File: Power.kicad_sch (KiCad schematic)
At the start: 1 part, among them U6 18650_DUAL_HOLDER

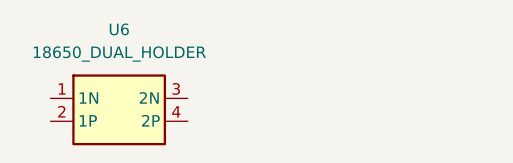
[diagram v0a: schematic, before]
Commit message: Receiver design
Updated the receiver design for the SX1280.
Added an ignore for lock files.
Minor schematic updates.
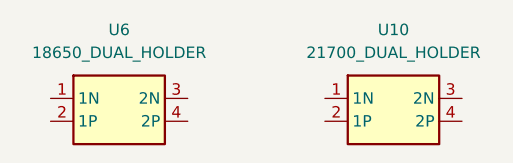
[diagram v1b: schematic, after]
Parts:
- added U10: 21700_DUAL_HOLDER, Custom_Parts:21700_DUAL_HOLDER, symbol Custom_Parts:21700_DUAL_HOLDER
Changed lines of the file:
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@@
+		)
+	)
+	(symbol
+		(lib_id "Custom_Parts:21700_DUAL_HOLDER")
+		(at 82.55 64.77 0)
+		(unit 1)
+		(exclude_from_sim no)
+		(in_bom yes)
+		(on_board yes)
+		(dnp no)
+		(fields_autoplaced yes)
+		(property "Reference" "U10"
+			(at 92.71 57.15 0)
+			(effects
+				(font
+					(size 1.27 1.27)
+				)
+			)
+		)
+		(property "Value" "21700_DUAL_HOLDER"
+			(at 92.71 59.69 0)
+			(effects
+				(font
+					(size 1.27 1.27)
+				)
+			)
+		)
+		(property "Footprint" "Custom_Parts:21700_DUAL_HOLDER"
+			(at 104.14 159.69 0)
+			(effects
+				(font
+					(size 1.27 1.27)
+				)
+				(justify left top)
+				(hide yes)
+			)
+		)
+		(property "Datasheet" "http://www.keyelco.com/product-pdf.cfm?p=920"
+			(at 104.14 259.69 0)
+			(effects
+				(font
+					(size 1.27 1.27)
+				)
+				(justify left top)
+				(hide yes)
+			)
+		)
+		(property "Description" "KEYSTONE - 1048 - BATTERY HOLDER, 18650 LI-ION, 2CELL, SMD"
+			(at 82.804 74.422 0)
+			(effects
+				(font
+					(size 1.27 1.27)
+				)
+				(hide yes)
+			)
+		)
+		(property "Height" ""
+			(at 104.14 459.69 0)
+			(effects
+				(font
+					(size 1.27 1.27)
+				)
+				(justify left top)
+				(hide yes)
+			)
+		)
+		(property "Mouser Part Number" "534-1048"
+			(at 104.14 559.69 0)
+			(effects
+				(font
+					(size 1.27 1.27)
+				)
+				(justify left top)
+				(hide yes)
+			)
+		)
+		(property "Mouser Price/Stock" "https://www.mouser.co.uk/ProductDetail/Keystone-Electronics/1048?qs=%2F7TOpeL5Mz5jXkg8vI8Dyw%3D%3D"
+			(at 104.14 659.69 0)
+			(effects
+				(font
+					(size 1.27 1.27)
+				)
+				(justify left top)
+				(hide yes)
+			)
+		)
+		(property "Manufacturer_Name" "Keystone Electronics"
+			(at 104.14 759.69 0)
+			(effects
+				(font
+					(size 1.27 1.27)
+				)
+				(justify left top)
+				(hide yes)
+			)
+		)
+		(property "Manufacturer_Part_Number" "1048"
+			(at 104.14 859.69 0)
+			(effects
+				(font
+					(size 1.27 1.27)
+				)
+				(justify left top)
+				(hide yes)
+			)
+		)
+		(pin "3"
+		)
+		(pin "2"
+		)
+		(pin "1"
+		)
+		(pin "4"
+		)
+		(instances
+			(project ""
+				(path "/ac187c6c-fa53-41cc-bce1-6f39a42a92e8/9df2a240-d97e-494f-85fd-6467f59fa68d"
+					(reference "U10")
+					(unit 1)
+				)
+			)
 		)
 	)

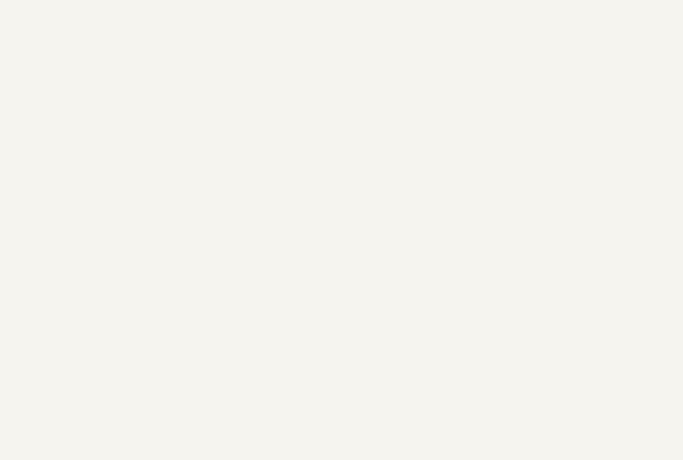
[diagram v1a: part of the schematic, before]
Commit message: Sensors design
Updated the inertial measurement unit schematic.
Updated the power monitor schematic.
Updated the barometer schematic.
Updated the receiver schematic.

TODO:
Review the sensors schematic.
Implement ESC schematic.
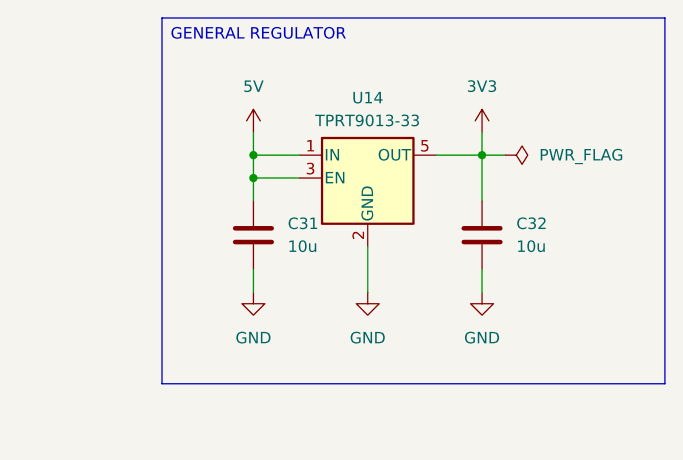
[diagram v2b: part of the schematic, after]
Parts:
- added C31, C32: 10u, symbol Device:C
- added U14: TPRT9013-33, Package_TO_SOT_SMD:SOT-23-5, symbol Regulator_Linear:TLV70233_SOT23-5
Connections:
- new net 3V3: C32.1, U14.5 (OUT)
- new net 5V: C31.1, U14.1 (IN), U14.3 (EN)
- new net GND: C31.2, C32.2, U14.2 (GND)

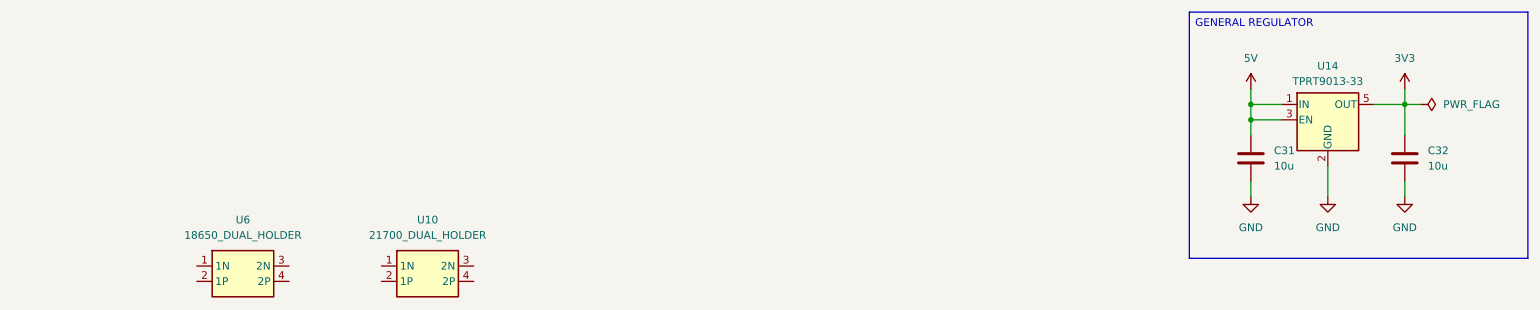
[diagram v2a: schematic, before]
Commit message: ESC design
Updated the ESC schematic.
Replaces the INA 226 with INA230.
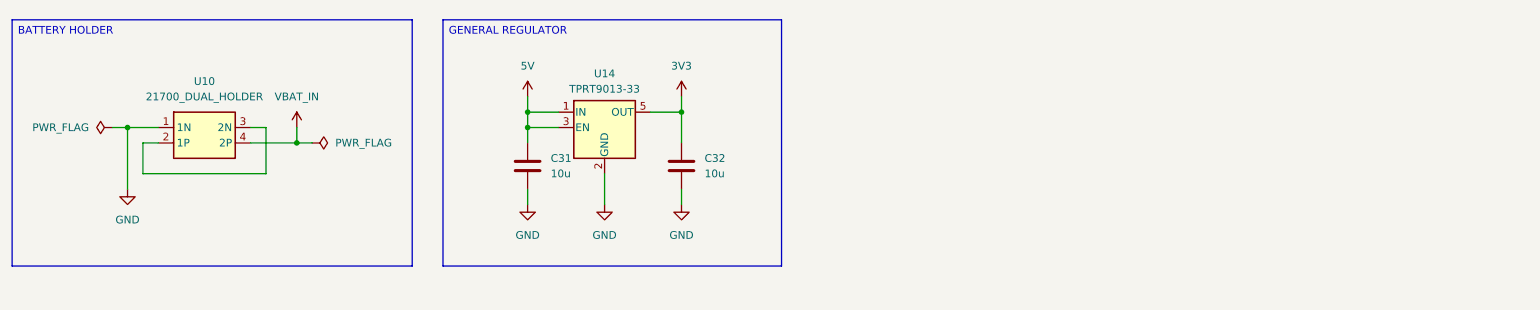
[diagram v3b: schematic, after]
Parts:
- removed U6: 18650_DUAL_HOLDER, Custom_Parts:18650_DUAL_HOLDER, symbol Custom_Parts:18650_DUAL_HOLDER
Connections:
- net GND: now also U10.1 (1N)
- net at U10.2 (1P): now also U10.3 (2N)
- net VBAT_IN: now reaches U10.4 (2P)
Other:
- moved on the sheet: C31, C32, U10, U14

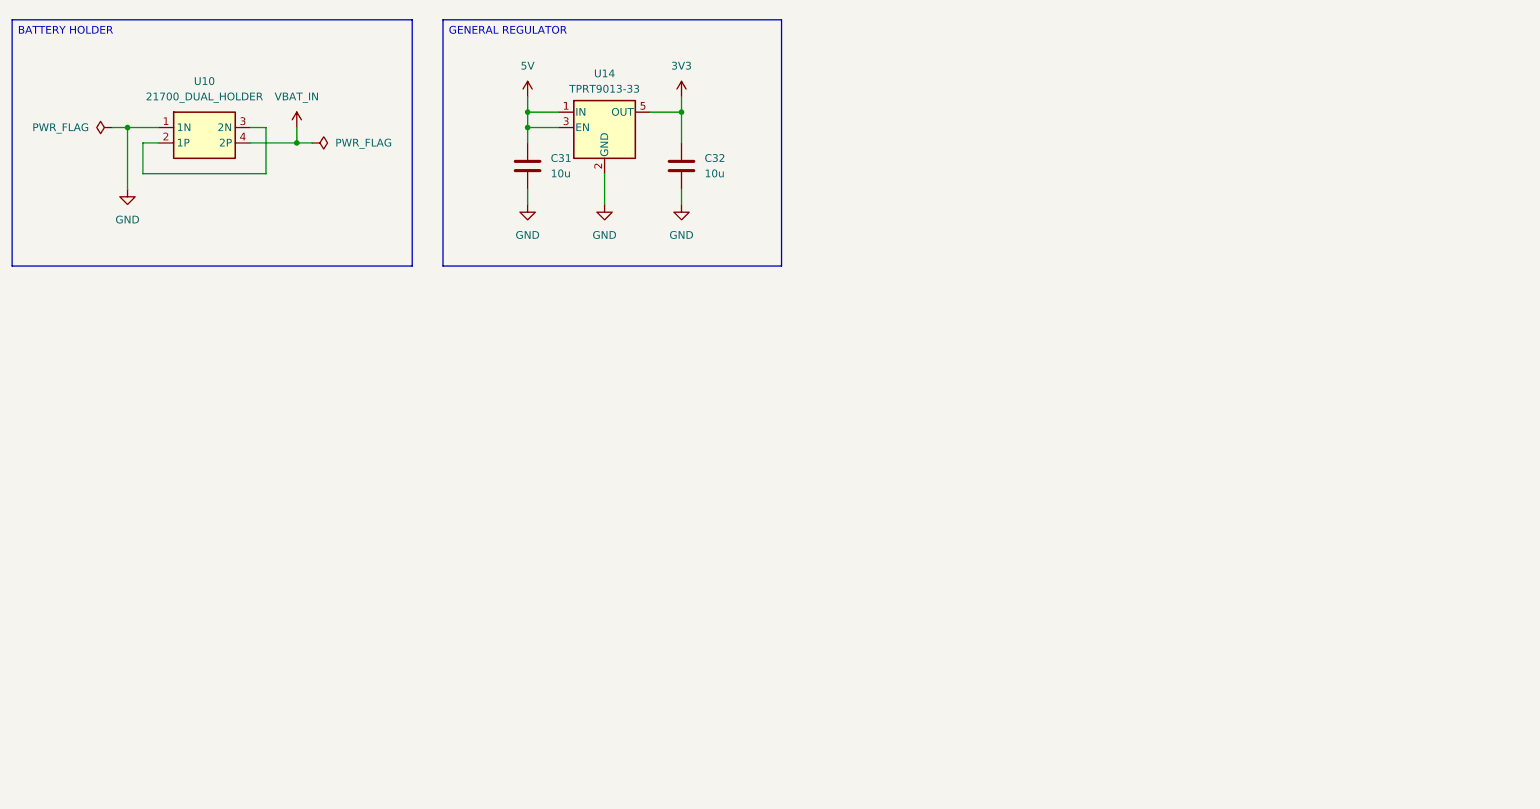
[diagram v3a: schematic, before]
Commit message: Power design
Added the 5V regulator schematic.
Updated the MCU schematic.
Updated the RX schematic.
Updated the sensors schematic.

TODO:
Calculate the voltage divider for the 5V regulator.
Review all connections and systems.
Select the footprints for the missing components.
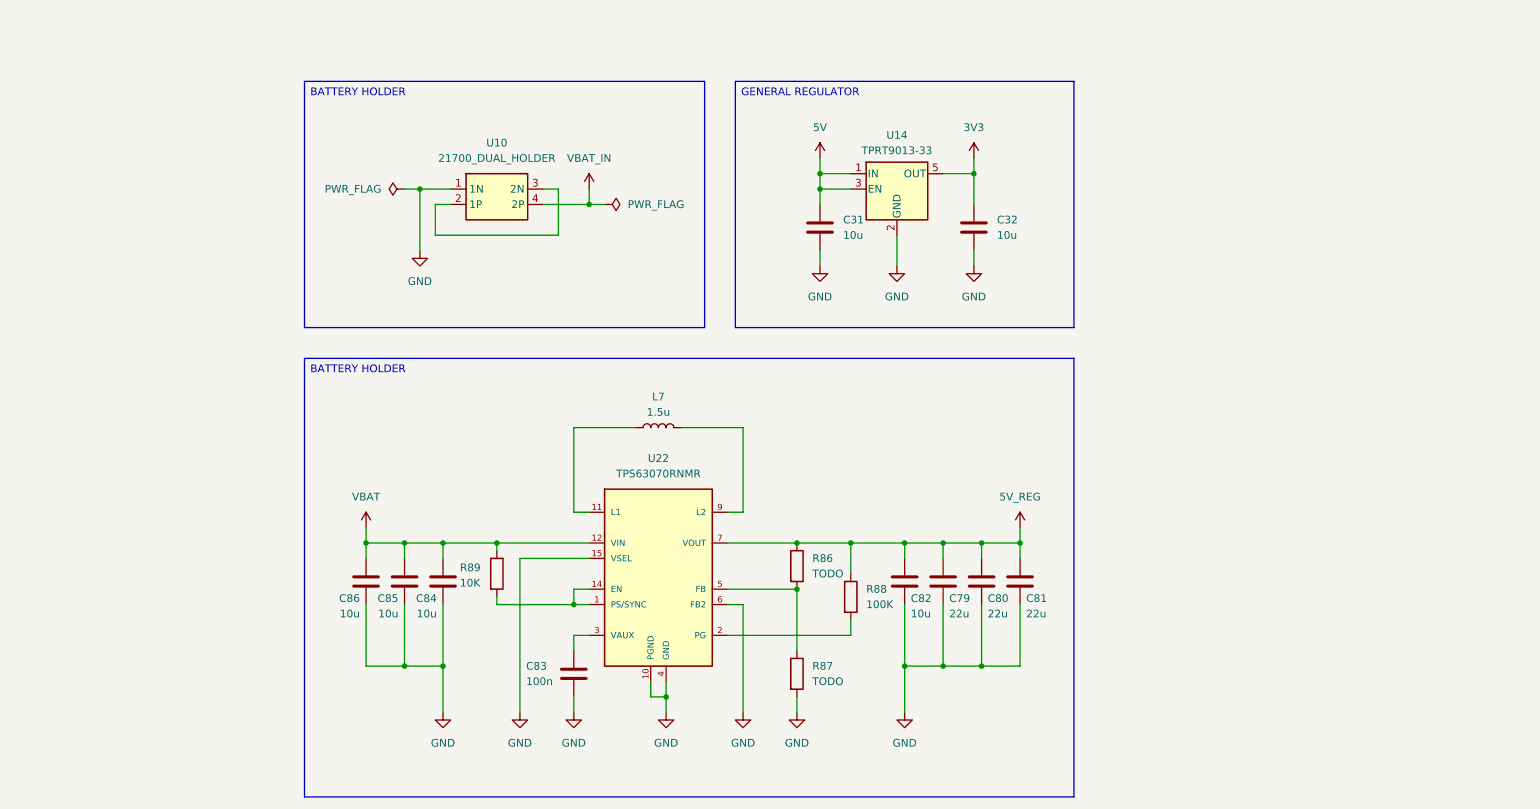
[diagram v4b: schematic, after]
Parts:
- added C79, C80, C81: 22u, symbol Device:C
- added C82, C84, C85, C86: 10u, symbol Device:C
- added C83: 100n, symbol Device:C
- added L7: 1.5u, symbol Device:L
- added R86, R87: TODO, symbol Device:R
- added R88: 100K, symbol Device:R
- added R89: 10K, symbol Device:R
- added U22: TPS63070RNMR, Custom_Parts:TPS63070RNMR, symbol Custom_Parts:TPS63070RNMR
- U10: footprint Custom_Parts:21700_DUAL_HOLDER -> Custom_Parts:21700_DUAL_HOLDER_MOUNTING
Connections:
- net GND: now also C79.2, C80.2, C81.2, C82.2, C83.2, C84.2, C85.2, C86.2, R87.2, U22.10 (PGND), U22.15 (VSEL), U22.4 (GND), U22.6 (FB2)
- new net: R89.2, U22.1 (PS/SYNC), U22.14 (EN)
- new net: L7.1, U22.11 (L1)
- new net: L7.2, U22.9 (L2)
- new net: R88.2, U22.2 (PG)
- new net: R86.2, R87.1, U22.5 (FB)
- new net: C83.1, U22.3 (VAUX)
- new net 5V_REG: C79.1, C80.1, C81.1, C82.1, R86.1, R88.1, U22.7 (VOUT)
- new net VBAT: C84.1, C85.1, C86.1, R89.1, U22.12 (VIN)
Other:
- moved on the sheet: C31, C32, U10, U14

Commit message: Footprints and revision
Added the missing footprints.
Updated a all the schematics.
Completed an initial review of the schematics.

TODO:
Perform a deep review of the schematics before committing to layout.
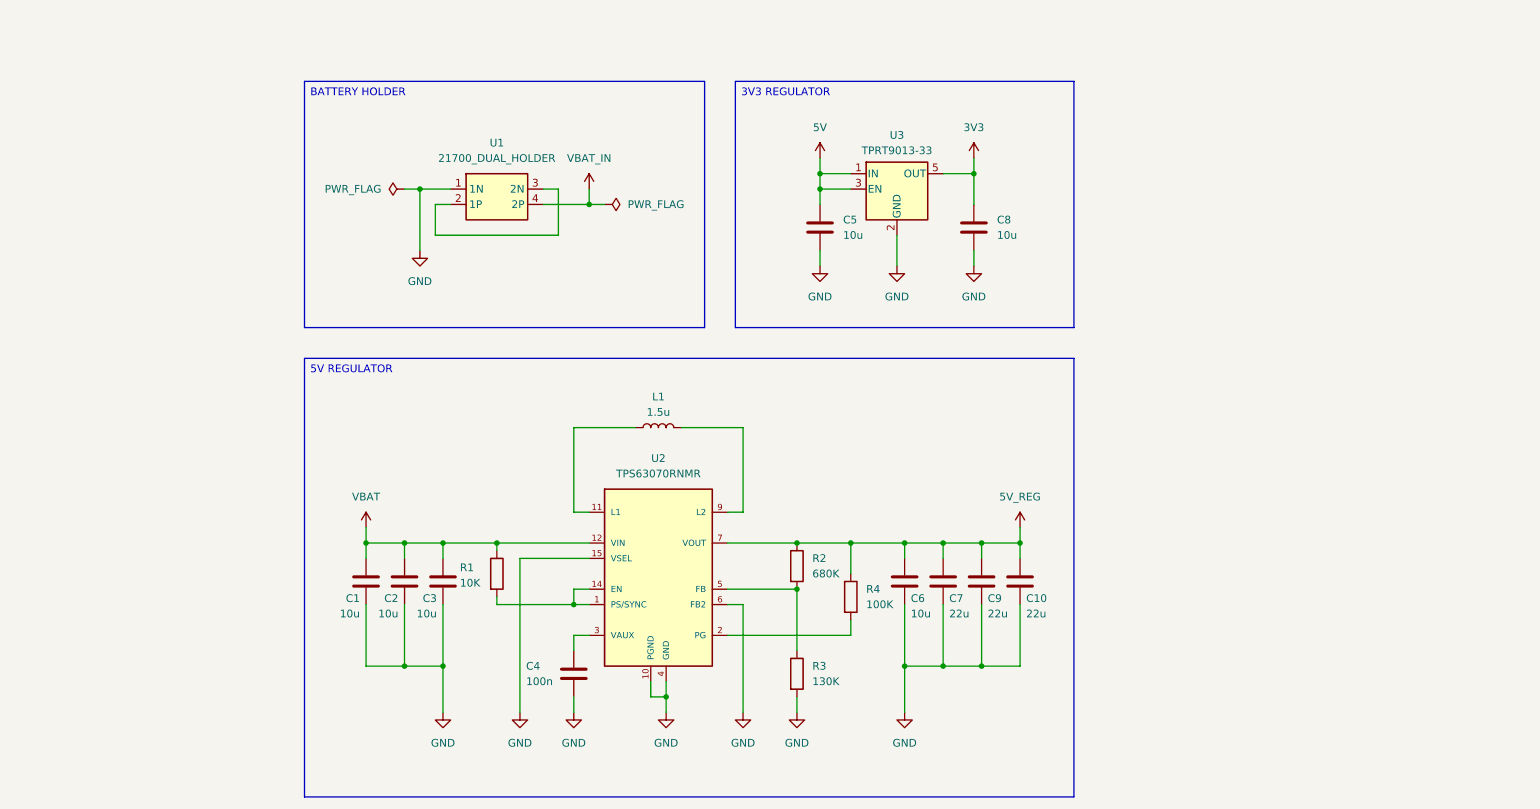
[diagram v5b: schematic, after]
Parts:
- C1: renamed from C86; footprint (none) -> Capacitor_SMD:C_0805_2012Metric
- C10: renamed from C81; footprint (none) -> Capacitor_SMD:C_1206_3216Metric
- C2: renamed from C85; footprint (none) -> Capacitor_SMD:C_0805_2012Metric
- C3: renamed from C84; footprint (none) -> Capacitor_SMD:C_0805_2012Metric
- C4: renamed from C83; footprint (none) -> Capacitor_SMD:C_0603_1608Metric
- C5: renamed from C31; footprint (none) -> Capacitor_SMD:C_0805_2012Metric
- C6: renamed from C82; footprint (none) -> Capacitor_SMD:C_0805_2012Metric
- C7: renamed from C79; footprint (none) -> Capacitor_SMD:C_1206_3216Metric
- C8: renamed from C32; footprint (none) -> Capacitor_SMD:C_0805_2012Metric
- C9: renamed from C80; footprint (none) -> Capacitor_SMD:C_1206_3216Metric
- L1: renamed from L7; footprint (none) -> Inductor_SMD:L_Panasonic_PCC-M0530M
- R1: renamed from R89; footprint (none) -> Resistor_SMD:R_0603_1608Metric
- R2: renamed from R86; value TODO -> 680K; footprint (none) -> Resistor_SMD:R_0603_1608Metric
- R3: renamed from R87; value TODO -> 130K; footprint (none) -> Resistor_SMD:R_0603_1608Metric
- R4: renamed from R88; footprint (none) -> Resistor_SMD:R_0603_1608Metric
- renumbered U10 to U1, U22 to U2, U14 to U3

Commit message: Power and MCU
Updated the power schematic.
Updated the MCU schematic.

TODO:
Merge with features branch.
Review all schematics prior to layout.
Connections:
- net EN: now reaches R1.2, U2.1 (PS/SYNC), U2.14 (EN)
- net L1: now reaches L1.1, U2.11 (L1)
- net L2: now reaches L1.2, U2.9 (L2)
- net PG: now reaches R4.2, U2.2 (PG)
- net FB: now reaches R2.2, R3.1, U2.5 (FB)
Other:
- company: Chapuzas S.L. -> DavidMolTor
